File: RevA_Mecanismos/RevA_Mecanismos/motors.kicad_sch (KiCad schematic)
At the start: 0 parts

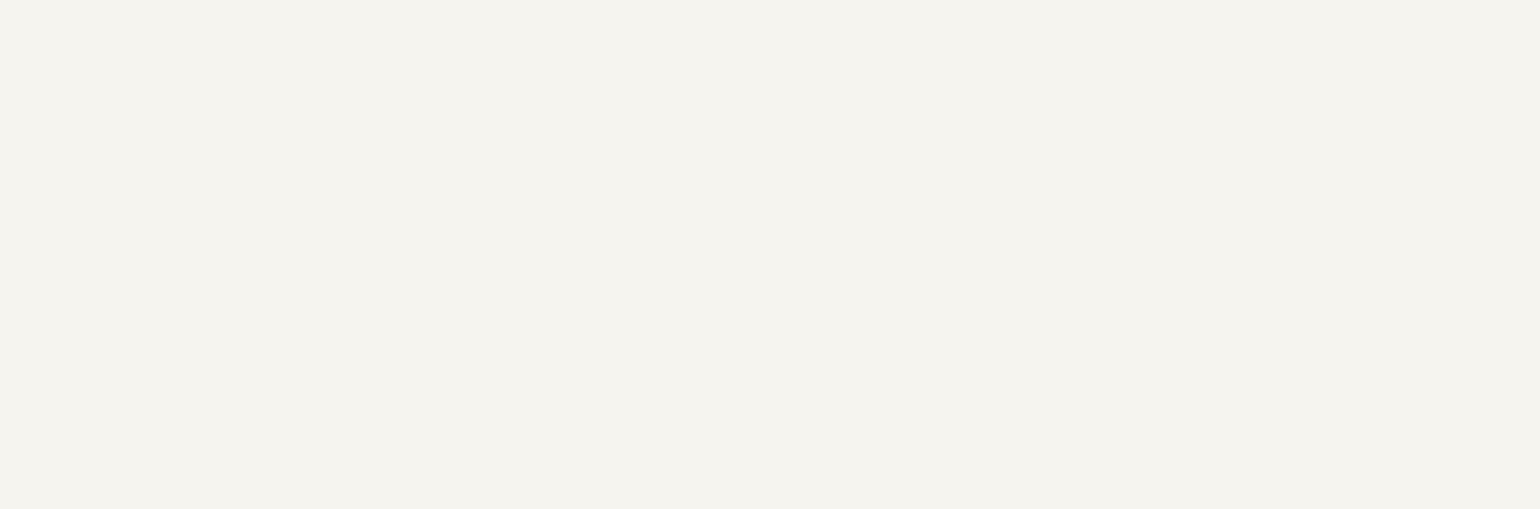
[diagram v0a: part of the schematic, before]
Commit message: Added H-Bridges and voltage regulators
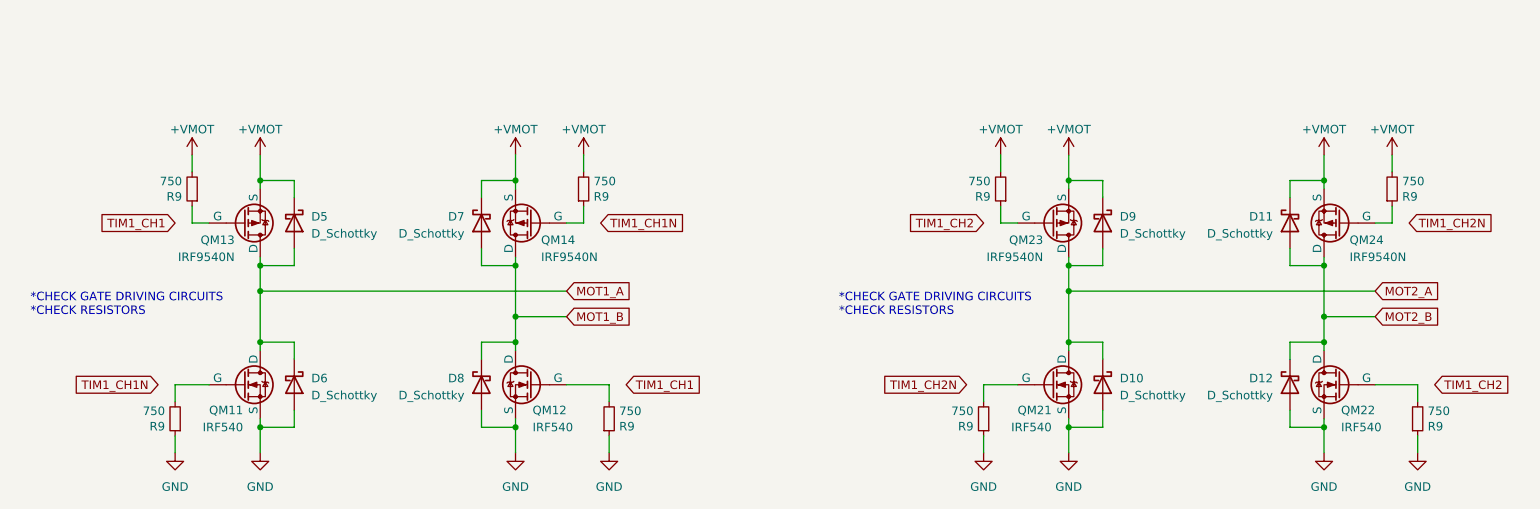
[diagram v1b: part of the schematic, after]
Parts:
- added D10, D11, D12, D5, D6, D7, D8, D9: D_Schottky, symbol Device:D_Schottky
- added QM11, QM12, QM21, QM22: IRF540, symbol Simulation_SPICE:NMOS
- added QM13, QM14, QM23, QM24: IRF9540N, symbol Simulation_SPICE:PMOS
- added R9 (x8): 750, Resistor_SMD:R_0603_1608Metric, symbol Device:R_Small
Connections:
- new net: QM22.2 (G), R9.2
- new net: QM11.2 (G), R9.2
- new net: QM14.2 (G), R9.1
- new net: QM24.2 (G), R9.1
- new net: QM21.2 (G), R9.2
- new net: QM23.2 (G), R9.1
- new net: QM13.2 (G), R9.1
- new net: QM12.2 (G), R9.2
- new net +VMOT: D11.1 (K), D5.1 (K), D7.1 (K), D9.1 (K), QM13.3 (S), QM14.3 (S), QM23.3 (S), QM24.3 (S), R9.2, R9.2, R9.2, R9.2
- new net GND: D10.2 (A), D12.2 (A), D6.2 (A), D8.2 (A), QM11.3 (S), QM12.3 (S), QM21.3 (S), QM22.3 (S), R9.1, R9.1, R9.1, R9.1
- new net MOT1_A: D5.2 (A), D6.1 (K), QM11.1 (D), QM13.1 (D)
- new net MOT1_B: D7.2 (A), D8.1 (K), QM12.1 (D), QM14.1 (D)
- new net MOT2_A: D10.1 (K), D9.2 (A), QM21.1 (D), QM23.1 (D)
- new net MOT2_B: D11.2 (A), D12.1 (K), QM22.1 (D), QM24.1 (D)
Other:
- note added: "*CHECK GATE DRIVING CIRCUITS *CHECK RESISTORS"

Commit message: Created PCB project
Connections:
- net TIM1_CH1: now also QM12.2 (G), QM13.2 (G), R9.1, R9.2
- net TIM1_CH1N: now also QM11.2 (G), QM14.2 (G), R9.1, R9.2
- net TIM1_CH2: now also QM22.2 (G), QM23.2 (G), R9.1, R9.2
- net TIM1_CH2N: now also QM21.2 (G), QM24.2 (G), R9.1, R9.2
- removed net +VMOT: D11.1 (K), D5.1 (K), D7.1 (K), D9.1 (K), QM13.3 (S), QM14.3 (S), QM23.3 (S), QM24.3 (S), R9.2, R9.2, R9.2, R9.2
- new net: D11.1 (K), QM24.3 (S)
- new net: D7.1 (K), QM14.3 (S)
- new net: D9.1 (K), QM23.3 (S)
- new net: D5.1 (K), QM13.3 (S)
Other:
- note added: "Motors"

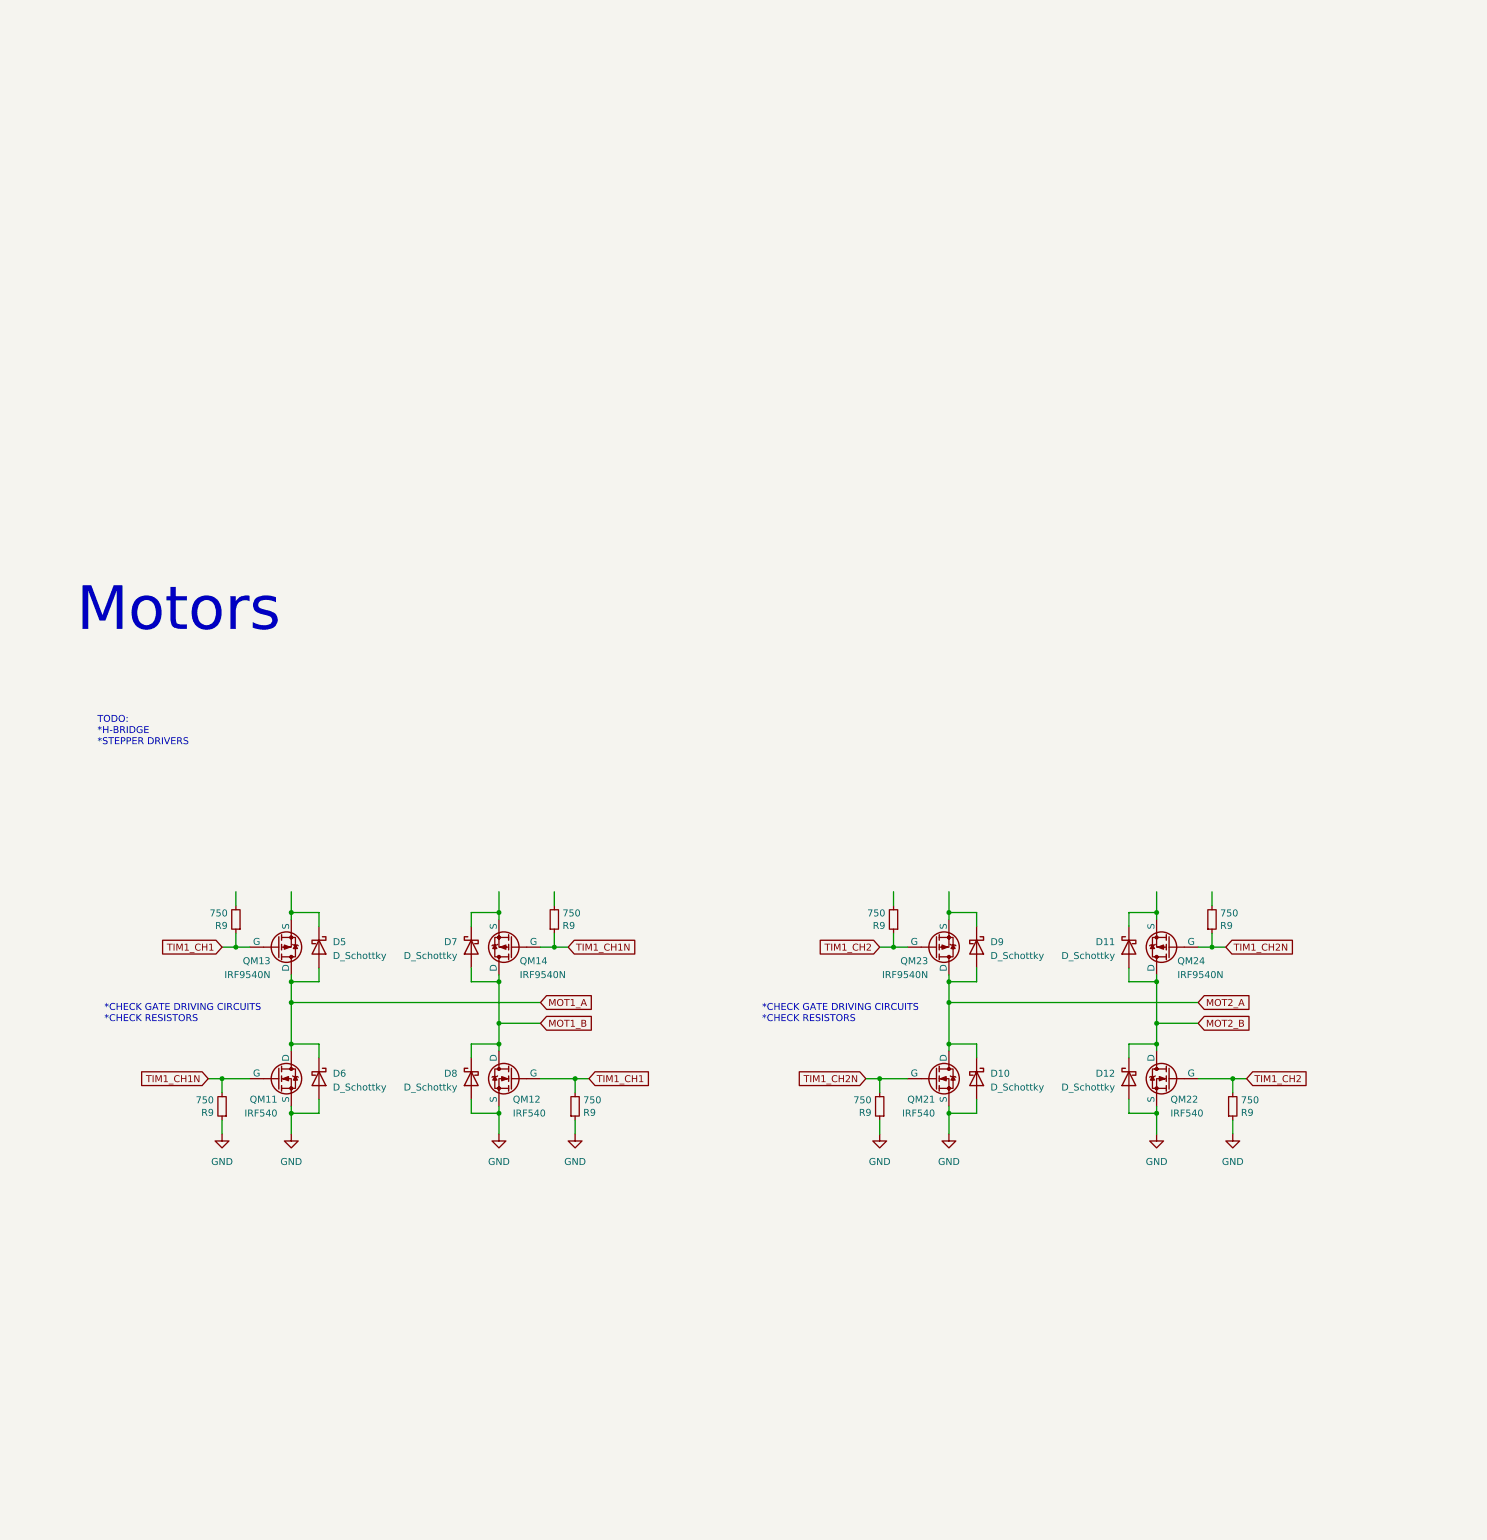
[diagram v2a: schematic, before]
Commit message: Adiciones a secciones de motores y power supply para placa de mecanismos
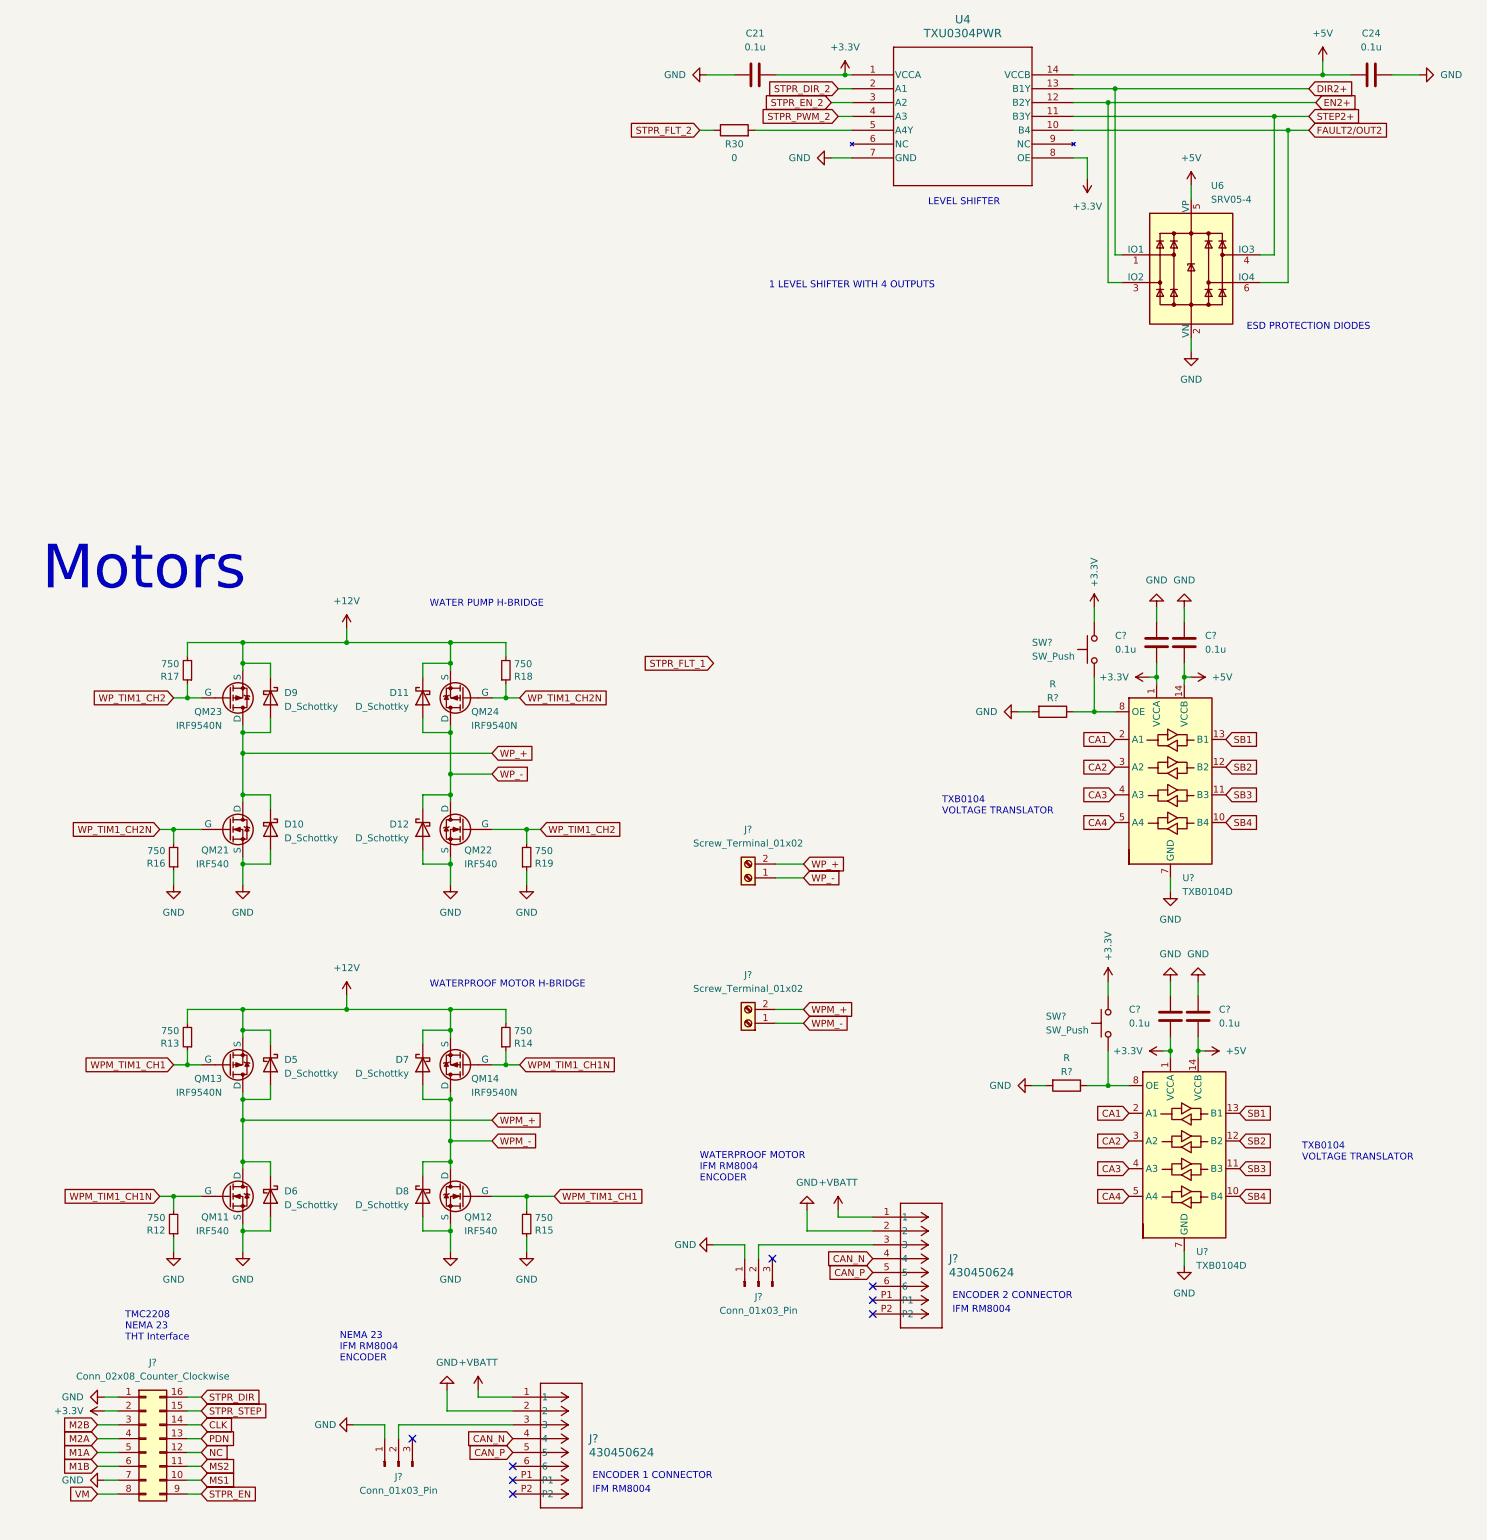
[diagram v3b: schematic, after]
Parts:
- added C21, C24, C? (x4): 0.1u, symbol Device:C
- added J? (x2): Screw_Terminal_01x02, TerminalBlock:TerminalBlock_Altech_AK300-2_P5.00mm, symbol Connector:Screw_Terminal_01x02
- added J? (x2): 430450624, CON_430450624_MOL, symbol MolexConnectors:430450624
- added J? (x2): Conn_01x03_Pin, symbol Connector:Conn_01x03_Pin
- added J?: Conn_02x08_Counter_Clockwise, Connector_PinHeader_2.54mm:PinHeader_2x08_P2.54mm_Vertical, symbol Connector_Generic:Conn_02x08_Counter_Clockwise
- added R30: 0, symbol Device:R
- added R? (x2): R, symbol Device:R
- added SW? (x2): SW_Push, symbol Switch:SW_Push
- added U4: TXU0304PWR, TSSOP14_PW_TEX, symbol TXU0304PWR:TXU0304PWR
- added U6: SRV05-4, Package_TO_SOT_SMD:SOT-23-6, symbol Power_Protection:SRV05-4
- added U? (x2): TXB0104D, Package_SO:SOIC-14_3.9x8.7mm_P1.27mm, symbol Logic_LevelTranslator:TXB0104D
- renumbered R9 to R12, R9 to R13, R9 to R14, R9 to R15, R9 to R16, R9 to R17, R9 to R18, R9 to R19
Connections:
- net GND: now also C21.1, C24.2, C?.1, C?.1, C?.1, C?.1, J?.1 (Pin_1), J?.1 (Pin_1), J?.1 (Pin_1), J?.2, J?.2, J?.7 (Pin_7), R?.2, R?.2, U4.7 (GND), U6.2 (VN), U?.7 (GND), U?.7 (GND)
- net +12V: now reaches R14.2
- net +12V: now also D11.1 (K), D5.1 (K), D7.1 (K), D9.1 (K), QM13.3 (S), QM14.3 (S), QM23.3 (S), QM24.3 (S), R13.2, R17.2, R18.2
- net MOT1_A renamed WPM_+
- net WPM_+: now also J?.2 (Pin_2)
- net MOT1_B renamed WPM_-
- net WPM_-: now also J?.1 (Pin_1)
- net MOT2_A renamed WP_+
- net WP_+: now also J?.2 (Pin_2)
- net MOT2_B renamed WP_-
- net WP_-: now also J?.1 (Pin_1)
- net TIM1_CH1 renamed WPM_TIM1_CH1
- net TIM1_CH1N renamed WPM_TIM1_CH1N
- net TIM1_CH2 renamed WP_TIM1_CH2
- net TIM1_CH2N renamed WP_TIM1_CH2N
- new net: J?.2 (Pin_2), J?.3 (x2)
- new net: R?.1, SW?.1, U?.8 (OE) (x2)
- new net: R30.2, U4.5 (A4Y)
- new net +3.3V: C21.2, C?.2, C?.2, J?.2 (Pin_2), SW?.2, SW?.2, U4.1 (VCCA), U4.8 (OE), U?.1 (VCCA), U?.1 (VCCA)
- new net +5V: C24.1, C?.2, C?.2, U4.14 (VCCB), U6.5 (VP), U?.14 (VCCB), U?.14 (VCCB)
- new net +VMOT: J?.1, J?.1
- new net CA1: U?.2 (A1), U?.2 (A1)
- new net CA2: U?.3 (A2), U?.3 (A2)
- new net CA3: U?.4 (A3), U?.4 (A3)
- new net CA4: U?.5 (A4), U?.5 (A4)
- new net CAN_N: J?.4, J?.4
- new net CAN_P: J?.5, J?.5
- new net CLK: J?.14 (Pin_14)
- new net DIR2+: U4.13 (B1Y), U6.1 (IO1)
- new net EN2+: U4.12 (B2Y), U6.3 (IO2)
- new net FAULT2/OUT2: U4.10 (B4), U6.6 (IO4)
- new net M1A: J?.5 (Pin_5)
- new net M1B: J?.6 (Pin_6)
- new net M2A: J?.4 (Pin_4)
- new net M2B: J?.3 (Pin_3)
- new net MS1: J?.10 (Pin_10)
- new net MS2: J?.11 (Pin_11)
- new net NC: J?.12 (Pin_12)
- new net PDN: J?.13 (Pin_13)
- new net SB1: U?.13 (B1), U?.13 (B1)
- new net SB2: U?.12 (B2), U?.12 (B2)
- new net SB3: U?.11 (B3), U?.11 (B3)
- new net SB4: U?.10 (B4), U?.10 (B4)
- new net STEP2+: U4.11 (B3Y), U6.4 (IO3)
- new net STPR_DIR: J?.16 (Pin_16)
- new net STPR_DIR_2: U4.2 (A1)
- new net STPR_EN: J?.9 (Pin_9)
- new net STPR_EN_2: U4.3 (A2)
- new net STPR_FLT_2: R30.1
- new net STPR_PWM_2: U4.4 (A3)
- new net STPR_STEP: J?.15 (Pin_15)
- new net VM: J?.8 (Pin_8)
- no-connect marks 0 -> 8
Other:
- note added: "1 LEVEL SHIFTER WITH 4 OUTPUTS"
- note added: "ENCODER 1 CONNECTOR"
- note added: "ENCODER 2 CONNECTOR"
- note added: "ESD PROTECTION DIODES"
- note added: "IFM RM8004"
- note added: "LEVEL SHIFTER"
- note added: "NEMA 23 IFM RM8004 ENCODER"
- note added: "TMC2208 NEMA 23 THT Interface"
- note added: "TXB0104 VOLTAGE TRANSLATOR"
- note added: "WATER PUMP H-BRIDGE"
- note added: "WATERPROOF MOTOR H-BRIDGE"
- note added: "WATERPROOF MOTOR IFM RM8004 ENCODER"
- note removed: "*CHECK GATE DRIVING CIRCUITS *CHECK RESISTORS"
- note removed: "TODO: *H-BRIDGE *STEPPER DRIVERS"
- moved on the sheet: D10, D11, D12, D5, D6, D7, D8, D9, QM11, QM12, QM13, QM14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
